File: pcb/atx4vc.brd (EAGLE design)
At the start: 69.4 x 69 mm, 38 parts, among them IC1 MY_7905DT, J2 ATX24RH

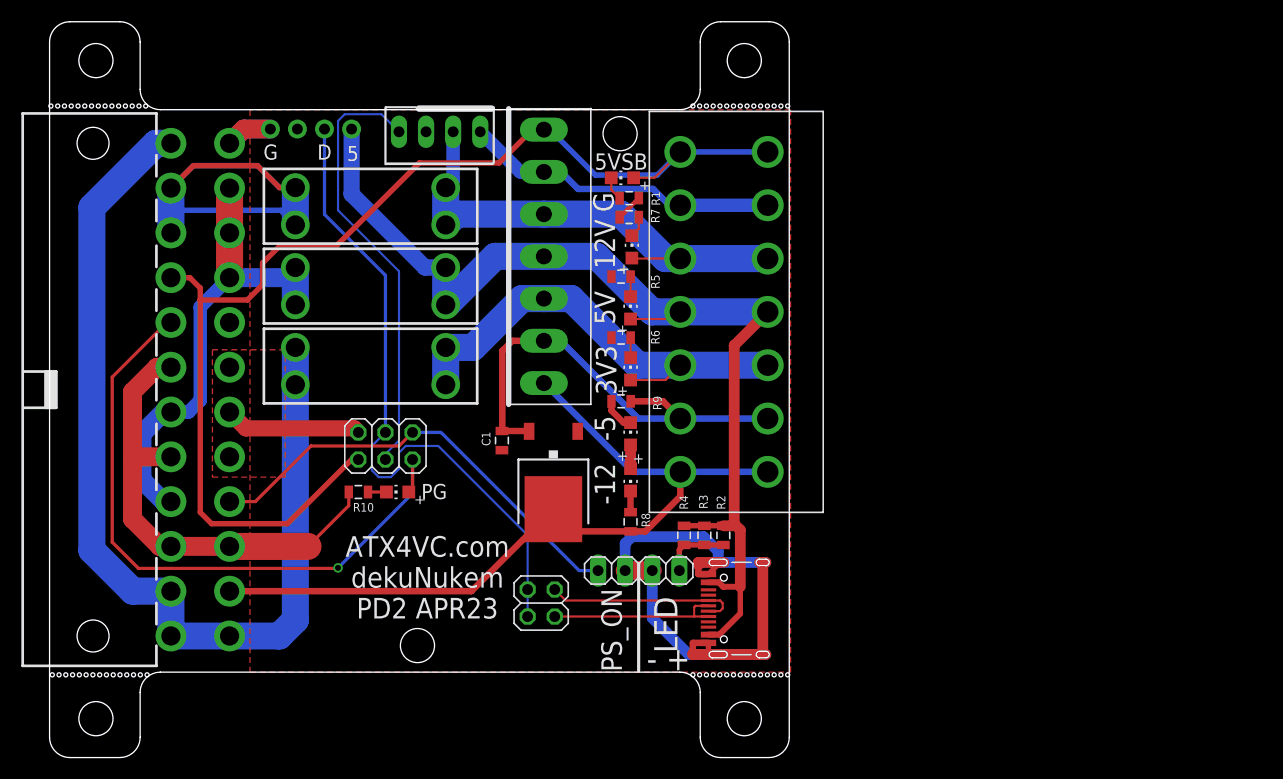
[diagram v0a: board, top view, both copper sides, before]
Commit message: added PG on terminal block, moved things around
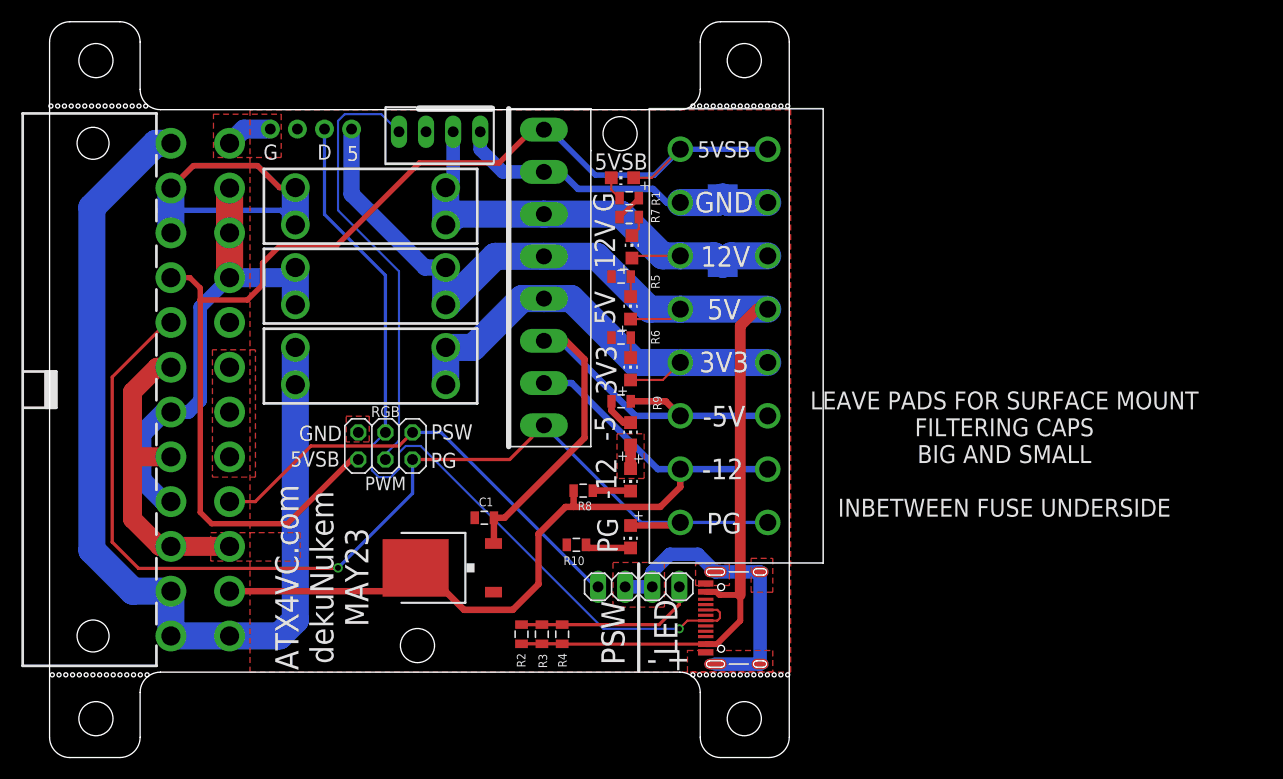
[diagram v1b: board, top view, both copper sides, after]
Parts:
- removed JP1: (no value), pinhead:2X02
- added C2: 470uF, rcl:SMC_D
- U$12: value DG2204R-5.0 -> DG2204R-5.0-8DG2204-8; device atx4vc:DG2204R -> atx4vc:DG2204R-8
- U$7: value VH396 -> VH396_8P; device 396_conn:396_7P -> 396_conn:396_8P
- moved LED7 22.2 mm to (54.5, 21.2), turned to 180 degrees
- moved R2 21.1 mm to (44.3, 12.1), turned to 270 degrees
- moved R10 21.0 mm to (49.4, 20.4)
- moved R3 17.8 mm to (46.2, 12.1), turned to 270 degrees
- moved R4 14.7 mm to (48.1, 12.1), turned to 270 degrees
- moved IC1 13.1 mm to (36.8, 18.3), turned to 90 degrees
- moved C1 7.43 mm to (40.8, 23.0), turned to 0 degrees
- moved R8 5.32 mm to (50.0, 25.5), turned to 0 degrees
- moved U$7 3.96 mm to (46.4, 43.5)
- moved JP2 1.52 mm to (57.8, 16.5)
- moved JP4 1.52 mm to (52.7, 16.5)
- moved J1 0.92 mm to (61.5, 13.6)
- moved U$12 0.25 mm to (63.2, 42.5)
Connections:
- removed net N$4: J1.A6, J1.B6, JP1.2
- removed net N$6: J1.A7, J1.B7, JP1.4
- net -12V: now also U$7.P$2; no longer U$7.P$1
- net -5V: now also U$7.P$3; no longer U$7.P$2
- net F12V: now also C2.+, U$7.P$6; no longer U$7.P$5
- net F3V3: now also U$7.P$4; no longer U$7.P$3
- net F5V: now also U$7.P$5; no longer U$7.P$4
- net GND: now also C2.-, U$7.P$7; no longer U$7.P$6
- net N$11: now also U$12.P$15, U$12.P$16, U$7.P$1
- net N$7: now also J1.A6, J1.B6; no longer JP1.1, JP1.3
- net VCC: now also U$7.P$8; no longer U$7.P$7
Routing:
- net GND: track 161.7 -> 98.7 mm
- net N$11: track 61.6 -> 101.6 mm
- net N$4: track 18.2 -> 0.00 mm
- net N$6: track 16.7 -> 0.00 mm
- net N$7: track 63.0 -> 79.4 mm, vias 0 -> 1
- net F5V: track 102.0 -> 116.1 mm
- net -5V: track 43.8 -> 55.0 mm
- net N$17: track 6.27 -> 17.2 mm
- net -12V: track 74.4 -> 79.9 mm
- net N$1: track 1.73 -> 4.30 mm
- net N$8: track 1.99 -> 3.56 mm
- net N$15: track 42.6 -> 43.2 mm
- net F12V: track 45.9 -> 46.5 mm
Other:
- board text added: "+"
- board text added: "-5V"
- board text added: "ATX4VC.com dekuNukem MAY23"
- board text added: "GND"
- board text added: "LEAVE PADS FOR SURFACE MOUNT FILTERING CAPS BIG AND SMALL INBETWEEN FUSE UNDERSIDE"
- board text added: "PSW"
- board text added: "PWM"
- board text added: "RGB"
- board text removed: "ATX4VC.com dekuNukem PD2 APR23"
- board text removed: "PS_ON"

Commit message: adding more caps
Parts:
- added C10, C4, C5, C6, C7, C8, C9: 2.2uF, atx_power_control:0805$1
- added C27: 47uF, clock:C1210
- added C3: 470uF, rcl:SMC_D
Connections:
- net -12V: now also C8.2
- net F12V: now also C6.2, C7.2
- net F3V3: now also C10.2, C27.1, C9.2
- net F5V: now also C3.+, C4.2, C5.2
- net GND: now also C10.1, C27.2, C3.-, C4.1, C5.1, C6.1, C7.1, C8.1, C9.1
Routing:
- net F12V: track 46.5 -> 53.5 mm
- net GND: track 98.7 -> 102.3 mm, vias 0 -> 1
- net F5V: track 116.1 -> 118.0 mm
- added copper zone on layer 16, net F3V3
- added copper zone on layer 16, net F5V
- added copper zone on layer 16, net GND
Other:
- board text added: "MAKE SURE CAPS ARE RATED FOR 12V"
- board text removed: "LEAVE PADS FOR SURFACE MOUNT FILTERING CAPS BIG AND SMALL INBETWEEN FUSE UNDERSIDE"

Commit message: adding more caps
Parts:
- added C11: 47uF, clock:C1210
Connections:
- net F12V: now also C11.1
- net GND: now also C11.2
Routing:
- net F12V: track 53.5 -> 56.5 mm
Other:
- board text added: "MAKE SURE TO USE 12V RATED CAPS ON 12V LINES"
- board text removed: "MAKE SURE CAPS ARE RATED FOR 12V"
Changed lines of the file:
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@@
 <grid distance="5" unitdist="mil" unit="mil" style="lines" multiple="1" display="no" altdistance="1" altunitdist="mil" altunit="mil"/>
 <layers>
-<layer number="1" name="Top" color="4" fill="1" visible="no" active="yes"/>
+<layer number="1" name="Top" color="4" fill="1" visible="yes" active="yes"/>
 <layer number="2" name="Route2" color="16" fill="1" visible="no" active="no"/>
 <layer number="3" name="Route3" color="17" fill="1" visible="no" active="no"/>
@@
 <layer number="19" name="Unrouted" color="6" fill="1" visible="yes" active="yes"/>
 <layer number="20" name="Dimension" color="24" fill="1" visible="yes" active="yes"/>
-<layer number="21" name="tPlace" color="7" fill="1" visible="no" active="yes"/>
-<layer number="22" name="bPlace" color="7" fill="1" visible="no" active="yes"/>
-<layer number="23" name="tOrigins" color="15" fill="1" visible="no" active="yes"/>
+<layer number="21" name="tPlace" color="7" fill="1" visible="yes" active="yes"/>
+<layer number="22" name="bPlace" color="7" fill="1" visible="yes" active="yes"/>
+<layer number="23" name="tOrigins" color="15" fill="1" visible="yes" active="yes"/>
 <layer number="24" name="bOrigins" color="15" fill="1" visible="yes" active="yes"/>
-<layer number="25" name="tNames" color="7" fill="1" visible="no" active="yes"/>
-<layer number="26" name="bNames" color="7" fill="1" visible="no" active="yes"/>
-<layer number="27" name="tValues" color="7" fill="1" visible="no" active="yes"/>
-<layer number="28" name="bValues" color="7" fill="1" visible="no" active="yes"/>
+<layer number="25" name="tNames" color="7" fill="1" visible="yes" active="yes"/>
+<layer number="26" name="bNames" color="7" fill="1" visible="yes" active="yes"/>
+<layer number="27" name="tValues" color="7" fill="1" visible="yes" active="yes"/>
+<layer number="28" name="bValues" color="7" fill="1" visible="yes" active="yes"/>
 <layer number="29" name="tStop" color="7" fill="3" visible="no" active="yes"/>
 <layer number="30" name="bStop" color="7" fill="6" visible="no" active="yes"/>
@@
 <layer number="37" name="tTest" color="7" fill="1" visible="no" active="yes"/>
 <layer number="38" name="bTest" color="7" fill="1" visible="no" active="yes"/>
-<layer number="39" name="tKeepout" color="4" fill="11" visible="no" active="yes"/>
+<layer number="39" name="tKeepout" color="4" fill="11" visible="yes" active="yes"/>
 <layer number="40" name="bKeepout" color="1" fill="11" visible="yes" active="yes"/>
-<layer number="41" name="tRestrict" color="4" fill="10" visible="no" active="yes"/>
+<layer number="41" name="tRestrict" color="4" fill="10" visible="yes" active="yes"/>
 <layer number="42" name="bRestrict" color="1" fill="10" visible="yes" active="yes"/>
 <layer number="43" name="vRestrict" color="2" fill="10" visible="no" active="yes"/>
@@
 <layer number="49" name="Reference" color="7" fill="1" visible="no" active="yes"/>
 <layer number="50" name="dxf" color="7" fill="1" visible="no" active="no"/>
-<layer number="51" name="tDocu" color="7" fill="1" visible="no" active="yes"/>
-<layer number="52" name="bDocu" color="7" fill="1" visible="no" active="yes"/>
+<layer number="51" name="tDocu" color="7" fill="1" visible="yes" active="yes"/>
+<layer number="52" name="bDocu" color="7" fill="1" visible="yes" active="yes"/>
 <layer number="53" name="tGND_GNDA" color="7" fill="1" visible="no" active="no"/>
 <layer number="54" name="bGND_GNDA" color="7" fill="1" visible="no" active="no"/>
@@
 <text x="31.496" y="26.2082" size="1.27" layer="25" rot="R180" align="center">PWM</text>
 <text x="31.496" y="32.9392" size="1.016" layer="25" rot="R180" align="center">RGB</text>
-<text x="88.9" y="35.687" size="1.6764" layer="25" align="center">MAKE SURE
-CAPS ARE RATED FOR 12V</text>
+<text x="93.091" y="36.703" size="1.6764" layer="25" align="center">MAKE SURE TO USE
+12V RATED CAPS ON 12V LINES</text>
 <text x="66.04" y="45.339" size="2.54" layer="26" rot="MR270" align="center">+</text>
+<text x="40.64" y="52.324" size="2.1844" layer="26" rot="MR0">+</text>
+<text x="28.575" y="48.26" size="2.1844" layer="26" rot="MR0">+</text>
 </plain>
 <attributes>
@@
 </element>
 <element name="C3" library="rcl" library_urn="urn:adsk.eagle:library:334" package="SMC_D" package3d_urn="urn:adsk.eagle:package:25923/2" value="470uF" x="30.226" y="46.101" smashed="yes" rot="MR270">
-<attribute name="NAME" x="27.686" y="48.641" size="1.016" layer="26" rot="MR270"/>
+<attribute name="NAME" x="28.194" y="44.069" size="1.016" layer="26" rot="MR270"/>
 <attribute name="POPULARITY" value="0" x="30.226" y="46.101" size="1.778" layer="28" rot="MR270" display="off"/>
 <attribute name="SPICEPREFIX" value="C" x="30.226" y="46.101" size="1.778" layer="28" rot="MR270" display="off"/>
 </element>
 <element name="C4" library="atx_power_control" package="0805$1" value="2.2uF" x="34.036" y="45.466" smashed="yes" rot="MR180">
-<attribute name="NAME" x="31.496" y="45.6565" size="0.8128" layer="26" rot="MR180"/>
+<attribute name="NAME" x="34.29" y="47.1805" size="0.8128" layer="26" rot="MR180"/>
 </element>
 <element name="C5" library="atx_power_control" package="0805$1" value="2.2uF" x="34.036" y="43.942" smashed="yes" rot="MR180">
-<attribute name="NAME" x="31.496" y="44.2595" size="0.8128" layer="26" rot="MR180"/>
+<attribute name="NAME" x="34.29" y="42.9895" size="0.8128" layer="26" rot="MR180"/>
 </element>
 <element name="C6" library="atx_power_control" package="0805$1" value="2.2uF" x="53.086" y="52.959" smashed="yes" rot="MR270">
-<attribute name="NAME" x="52.1335" y="54.61" size="0.8128" layer="26" rot="MR270"/>
+<attribute name="NAME" x="53.5305" y="55.626" size="0.8128" layer="26" rot="MR270"/>
 </element>
 <element name="C7" library="atx_power_control" package="0805$1" value="2.2uF" x="51.181" y="52.959" smashed="yes" rot="MR270">
-<attribute name="NAME" x="50.2285" y="54.61" size="0.8128" layer="26" rot="MR270"/>
+<attribute name="NAME" x="51.6255" y="55.626" size="0.8128" layer="26" rot="MR270"/>
 </element>
 <element name="C8" library="atx_power_control" package="0805$1" value="2.2uF" x="29.718" y="15.24" smashed="yes" rot="R90">
@@
 </element>
 <element name="C27" library="clock" package="C1210" value="47uF" x="32.512" y="39.116" smashed="yes" rot="MR0">
-<attribute name="NAME" x="34.163" y="36.576" size="0.8128" layer="26" rot="MR0"/>
+<attribute name="NAME" x="29.591" y="38.481" size="0.8128" layer="26" rot="MR0"/>
 </element>
 <element name="C9" library="atx_power_control" package="0805$1" value="2.2uF" x="32.639" y="36.576" smashed="yes" rot="MR180">
-<attribute name="NAME" x="30.988" y="35.6235" size="0.8128" layer="26" rot="MR180"/>
+<attribute name="NAME" x="29.718" y="36.8935" size="0.8128" layer="26" rot="MR180"/>
 </element>
 <element name="C10" library="atx_power_control" package="0805$1" value="2.2uF" x="32.639" y="34.925" smashed="yes" rot="MR180">
-<attribute name="NAME" x="30.988" y="33.9725" size="0.8128" layer="26" rot="MR180"/>
+<attribute name="NAME" x="28.956" y="35.4965" size="0.8128" layer="26" rot="MR180"/>
+</element>
+<element name="C11" library="clock" package="C1210" value="47uF" x="41.148" y="55.626" smashed="yes" rot="MR180">
+<attribute name="NAME" x="42.037" y="53.848" size="0.8128" layer="26" rot="MR180"/>
 </element>
 </elements>
@@
 <wire x1="11.379" y1="28.7" x2="7.781" y2="28.7" width="1.778" layer="1"/>
 <wire x1="7.781" y1="28.7" x2="7.779" y2="28.702" width="1.778" layer="1"/>
-<wire x1="42.499" y1="55.418" x2="40.386" y2="57.531" width="1.27" layer="16"/>
-<wire x1="40.386" y1="57.531" x2="40.386" y2="59.182" width="1.27" layer="16"/>
 <wire x1="47.96" y1="55.418" x2="49.5554" y2="53.8226" width="0.6096" layer="16"/>
 <wire x1="49.5554" y1="53.8226" x2="56.5984" y2="53.8226" width="0.6096" layer="16"/>
@@
 <contactref element="U$7" pad="P$7"/>
 <wire x1="46.355" y1="55.418" x2="47.96" y2="55.418" width="0.6096" layer="16"/>
-<wire x1="46.355" y1="55.418" x2="42.499" y2="55.418" width="1.27" layer="16"/>
 <polygon width="0.1524" layer="1" thermals="no">
 <vertex x="60.579" y="18.669"/>
@@
 <vertex x="32.639" y="46.228"/>
 </polygon>
+<contactref element="C11" pad="2"/>
+<wire x1="40.386" y1="59.182" x2="40.64" y2="59.182" width="1.27" layer="16"/>
+<wire x1="42.548" y1="57.274" x2="42.548" y2="55.626" width="1.27" layer="16"/>
+<wire x1="40.64" y1="59.182" x2="42.548" y2="57.274" width="1.27" layer="16"/>
+<wire x1="42.548" y1="55.626" x2="46.147" y2="55.626" width="1.27" layer="16"/>
+<wire x1="46.147" y1="55.626" x2="46.355" y2="55.418" width="1.27" layer="16"/>
 </signal>
 <signal name="N$5">
@@
 <wire x1="59.146" y1="47.545" x2="54.816" y2="47.545" width="0.2032" layer="1"/>
 <wire x1="54.608" y1="47.337" x2="54.816" y2="47.545" width="0.2032" layer="1"/>
-<wire x1="37.846" y1="59.182" x2="37.846" y2="54.644" width="1.27" layer="16"/>
-<wire x1="37.149" y1="53.947" x2="37.846" y2="54.644" width="1.27" layer="16"/>
 <contactref element="U$7" pad="P$6"/>
-<wire x1="38.16" y1="51.458" x2="46.355" y2="51.458" width="2.54" layer="16"/>
+<wire x1="38.16" y1="51.458" x2="39.751" y2="51.458" width="2.54" layer="16"/>
+<wire x1="39.751" y1="51.458" x2="46.355" y2="51.458" width="2.54" layer="16"/>
 <wire x1="46.355" y1="51.458" x2="53.571" y2="51.458" width="2.54" layer="16"/>
 <contactref element="C2" pad="+"/>
@@
 <wire x1="51.181" y1="52.059" x2="50.58" y2="51.458" width="0.2032" layer="16"/>
 <wire x1="50.58" y1="51.458" x2="46.355" y2="51.458" width="0.2032" layer="16"/>
+<contactref element="C11" pad="1"/>
+<wire x1="39.748" y1="55.626" x2="39.748" y2="51.461" width="1.27" layer="16"/>
+<wire x1="39.748" y1="51.461" x2="39.751" y2="51.458" width="1.27" layer="16"/>
+<wire x1="39.748" y1="55.626" x2="37.846" y2="57.528" width="1.27" layer="16"/>
+<wire x1="37.846" y1="57.528" x2="37.846" y2="59.182" width="1.27" layer="16"/>
 </signal>
 <signal name="F3V3">

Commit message: new run
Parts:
- moved C11 1.42 mm to (41.4, 54.2), turned to 90 degrees
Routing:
- net F12V: track 56.5 -> 43.9 mm
- net N$10: track 45.7 -> 47.8 mm
- net GND: track 102.3 -> 102.8 mm
- added copper zone on layer 16, net F12V
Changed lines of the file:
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@@
 <circle x="4.318" y="65.786" radius="4" width="0" layer="42"/>
 <circle x="65.153" y="65.913" radius="4" width="0" layer="42"/>
-<text x="24.638" y="17.399" size="2.1844" layer="25" rot="R90" align="center">ATX4VC.com
+<text x="24.13" y="17.399" size="2.1844" layer="25" rot="R90" align="center">ATX4VC.com
 dekuNukem
 MAY23</text>
@@
 12V RATED CAPS ON 12V LINES</text>
 <text x="66.04" y="45.339" size="2.54" layer="26" rot="MR270" align="center">+</text>
-<text x="40.64" y="52.324" size="2.1844" layer="26" rot="MR0">+</text>
+<text x="42.164" y="49.53" size="2.1844" layer="26" rot="MR0">+</text>
 <text x="28.575" y="48.26" size="2.1844" layer="26" rot="MR0">+</text>
 </plain>
@@
 <attribute name="NAME" x="28.956" y="35.4965" size="0.8128" layer="26" rot="MR180"/>
 </element>
-<element name="C11" library="clock" package="C1210" value="47uF" x="41.148" y="55.626" smashed="yes" rot="MR180">
-<attribute name="NAME" x="42.037" y="53.848" size="0.8128" layer="26" rot="MR180"/>
+<element name="C11" library="clock" package="C1210" value="47uF" x="41.402" y="54.229" smashed="yes" rot="MR90">
+<attribute name="NAME" x="43.307" y="57.023" size="0.8128" layer="26" rot="MR0"/>
 </element>
 </elements>
@@
 </polygon>
 <polygon width="0.1524" layer="1" thermals="no">
-<vertex x="29.972" y="30.099"/>
-<vertex x="27.813" y="30.099"/>
-<vertex x="27.813" y="32.512"/>
-<vertex x="29.972" y="32.512"/>
+<vertex x="29.972" y="30.353"/>
+<vertex x="27.813" y="30.353"/>
+<vertex x="27.813" y="32.131"/>
+<vertex x="29.972" y="32.131"/>
 </polygon>
 <contactref element="C2" pad="-"/>
@@
 </polygon>
 <contactref element="C11" pad="2"/>
-<wire x1="40.386" y1="59.182" x2="40.64" y2="59.182" width="1.27" layer="16"/>
-<wire x1="42.548" y1="57.274" x2="42.548" y2="55.626" width="1.27" layer="16"/>
-<wire x1="40.64" y1="59.182" x2="42.548" y2="57.274" width="1.27" layer="16"/>
-<wire x1="42.548" y1="55.626" x2="46.147" y2="55.626" width="1.27" layer="16"/>
-<wire x1="46.147" y1="55.626" x2="46.355" y2="55.418" width="1.27" layer="16"/>
+<wire x1="40.386" y1="59.182" x2="40.386" y2="56.645" width="1.524" layer="16"/>
+<wire x1="40.386" y1="56.645" x2="41.402" y2="55.629" width="1.524" layer="16"/>
+<wire x1="46.355" y1="55.418" x2="46.144" y2="55.629" width="1.524" layer="16"/>
+<wire x1="46.144" y1="55.629" x2="41.402" y2="55.629" width="1.524" layer="16"/>
 </signal>
 <signal name="N$5">
@@
 <wire x1="13.03" y1="32.9" x2="11.379" y2="32.9" width="1.27" layer="16"/>
 <wire x1="14.129" y1="42.75" x2="14.129" y2="33.999" width="1.27" layer="16"/>
-<wire x1="11.379" y1="32.9" x2="10.707" y2="32.9" width="1.778" layer="16"/>
-<wire x1="10.707" y1="32.9" x2="8.668" y2="30.861" width="1.778" layer="16"/>
-<wire x1="8.668" y1="30.861" x2="8.668" y2="26.543" width="1.778" layer="16"/>
-<wire x1="10.711" y1="24.5" x2="11.379" y2="24.5" width="1.778" layer="16"/>
-<wire x1="8.668" y1="26.543" x2="10.711" y2="24.5" width="1.778" layer="16"/>
+<wire x1="11.379" y1="32.9" x2="9.437" y2="32.9" width="1.778" layer="16"/>
+<wire x1="9.437" y1="32.9" x2="8.033" y2="31.496" width="1.778" layer="16"/>
+<wire x1="8.033" y1="31.496" x2="8.033" y2="25.908" width="1.778" layer="16"/>
+<wire x1="9.441" y1="24.5" x2="11.379" y2="24.5" width="1.778" layer="16"/>
+<wire x1="8.033" y1="25.908" x2="9.441" y2="24.5" width="1.778" layer="16"/>
 <wire x1="16.879" y1="53.9" x2="16.879" y2="49.7" width="2.54" layer="1"/>
 <wire x1="16.879" y1="49.7" x2="16.879" y2="45.5" width="2.54" layer="1"/>
@@
 <polygon width="0.1524" layer="16" thermals="no">
 <vertex x="34.544" y="47.752"/>
-<vertex x="34.544" y="44.069"/>
-<vertex x="37.338" y="44.069"/>
+<vertex x="34.544" y="43.434"/>
+<vertex x="37.338" y="43.434"/>
 <vertex x="37.338" y="47.752"/>
 </polygon>
@@
 <contactref element="JP5" pad="2"/>
 <wire x1="37.149" y1="53.947" x2="37.149" y2="50.447" width="2.54" layer="16"/>
-<wire x1="37.149" y1="50.447" x2="38.16" y2="51.458" width="2.54" layer="16"/>
 <contactref element="U$12" pad="P$6"/>
 <contactref element="U$12" pad="P$5"/>
@@
 <wire x1="54.608" y1="47.337" x2="54.816" y2="47.545" width="0.2032" layer="1"/>
 <contactref element="U$7" pad="P$6"/>
-<wire x1="38.16" y1="51.458" x2="39.751" y2="51.458" width="2.54" layer="16"/>
-<wire x1="39.751" y1="51.458" x2="46.355" y2="51.458" width="2.54" layer="16"/>
 <wire x1="46.355" y1="51.458" x2="53.571" y2="51.458" width="2.54" layer="16"/>
 <contactref element="C2" pad="+"/>
@@
 <wire x1="50.58" y1="51.458" x2="46.355" y2="51.458" width="0.2032" layer="16"/>
 <contactref element="C11" pad="1"/>
-<wire x1="39.748" y1="55.626" x2="39.748" y2="51.461" width="1.27" layer="16"/>
-<wire x1="39.748" y1="51.461" x2="39.751" y2="51.458" width="1.27" layer="16"/>
-<wire x1="39.748" y1="55.626" x2="37.846" y2="57.528" width="1.27" layer="16"/>
-<wire x1="37.846" y1="57.528" x2="37.846" y2="59.182" width="1.27" layer="16"/>
+<wire x1="37.846" y1="59.182" x2="37.846" y2="54.644" width="1.524" layer="16"/>
+<wire x1="37.846" y1="54.644" x2="37.149" y2="53.947" width="1.524" layer="16"/>
+<polygon width="0.1524" layer="16" thermals="no">
+<vertex x="42.799" y="53.594"/>
+<vertex x="43.688" y="52.705"/>
+<vertex x="47.752" y="52.705"/>
+<vertex x="47.752" y="50.292"/>
+<vertex x="41.91" y="50.292"/>
+<vertex x="41.275" y="50.927"/>
+<vertex x="35.941" y="50.927"/>
+<vertex x="35.941" y="53.594"/>
+</polygon>
 </signal>
 <signal name="F3V3">
